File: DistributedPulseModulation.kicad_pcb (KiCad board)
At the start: 2 copper layers, 95.9 x 90.2 mm, 67 parts, among them J1 Conn_02x12_Odd_Even, J2 Conn_01x01, U1 74LS251, U10 4053, U11 4053, U12 4053, U2 74LVC2G74, U25 74LS85, U28 74LS85, U31 74LS85, U4 MCP23017_SP, U7 4053, U8 4040, U9 4040

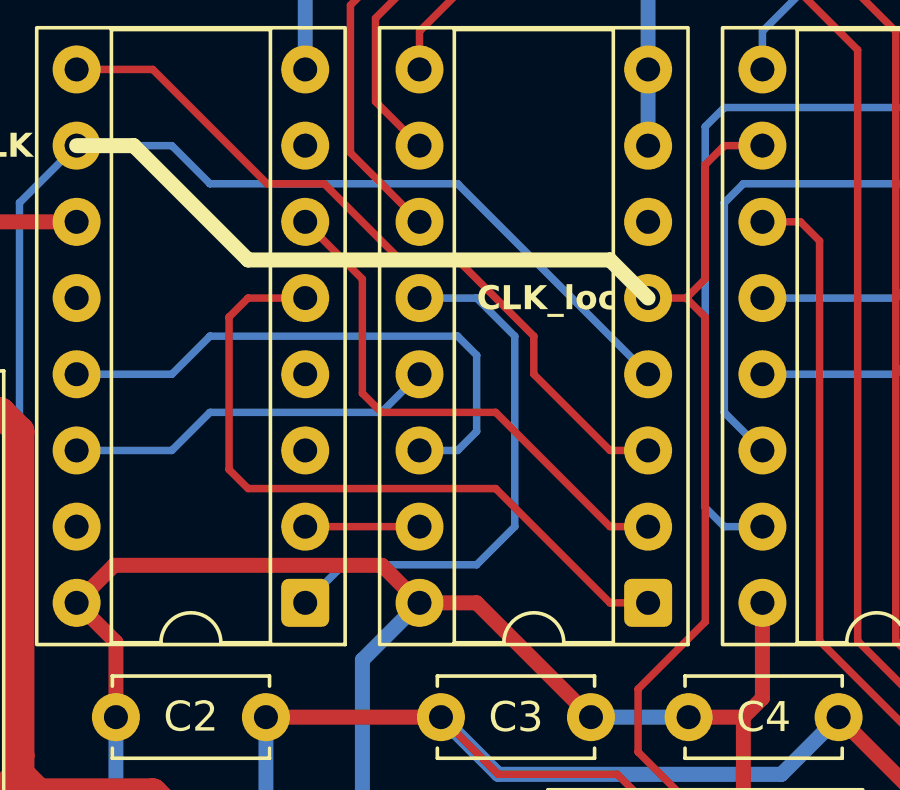
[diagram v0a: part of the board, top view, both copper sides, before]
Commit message: [UPGRADE] : ajout R6 pour pb tension entre TTL et CMOS - A jout de R6 (2.2K) en pull-uup sur la pin 5 du 74ls251 (TTL) en entrée du 74HCT4040 (CMOS)
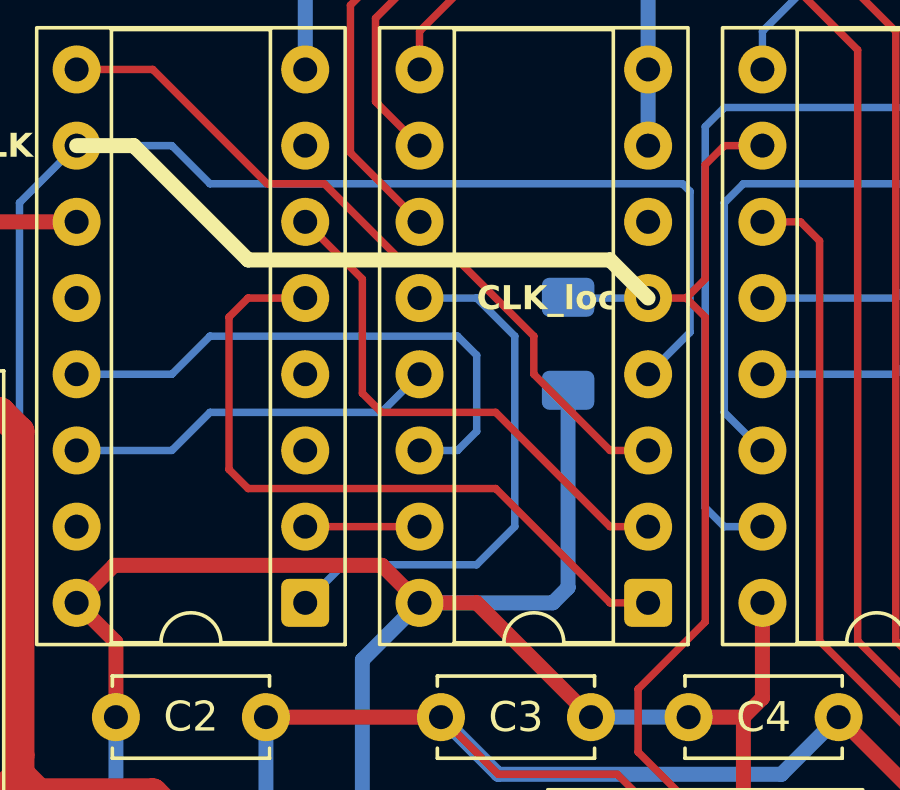
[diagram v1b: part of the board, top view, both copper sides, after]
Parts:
- added R6: 2.2K, Resistor_SMD:R_1206_3216Metric_Pad1.30x1.75mm_HandSolder, B.Cu at (69.1, 62.5)
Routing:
- net +5V: track 521.9 -> 533.6 mm
- net Clock: track 47.9 -> 53.5 mm
- net /Clock_loc: track 82.5 -> 85.2 mm

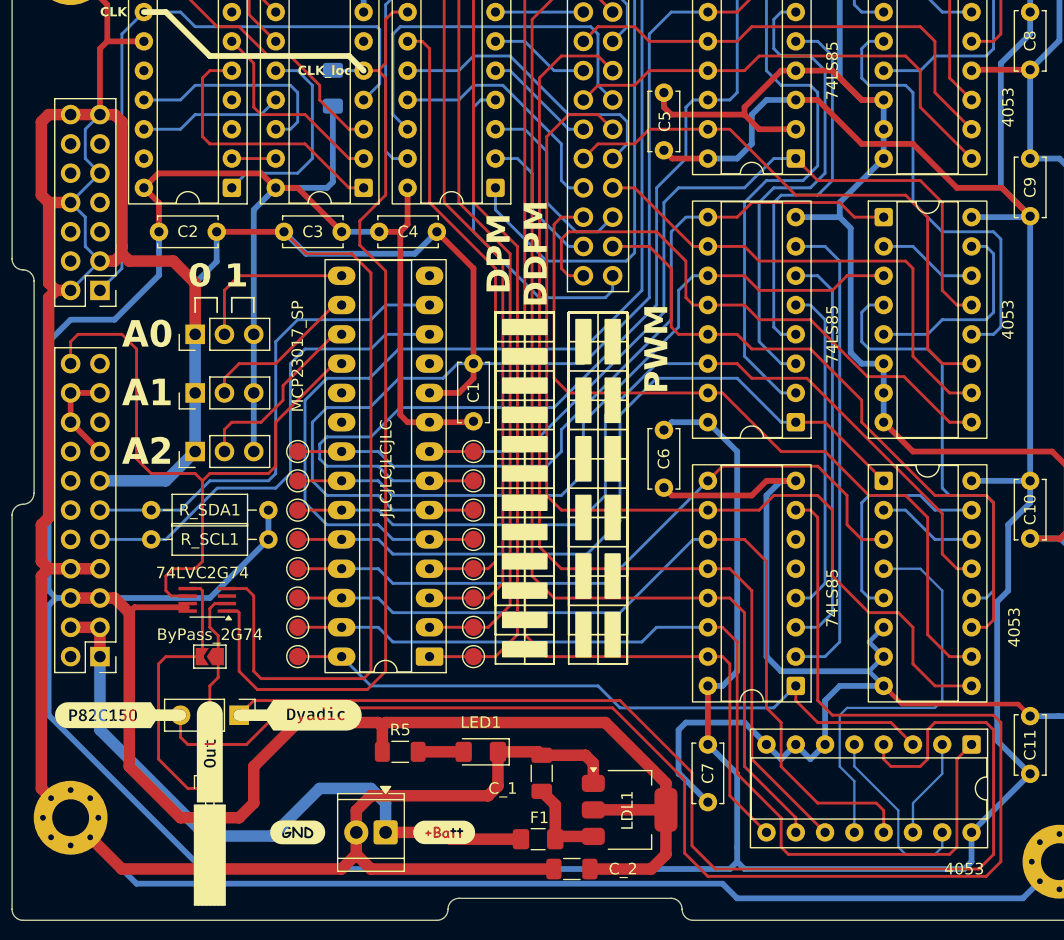
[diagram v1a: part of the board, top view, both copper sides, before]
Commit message: [UPGRADE] : ajout R7 pour pb tension entre TTL et CMOS - A jout de R7 (2.2K) en pull-up sur la sortie finale de la carte
[TODO]
-> adding replacement circuit for Dlatch chip
-> remove supply voltage regulator from PCB

[DONE]
-> correction voltage bugs
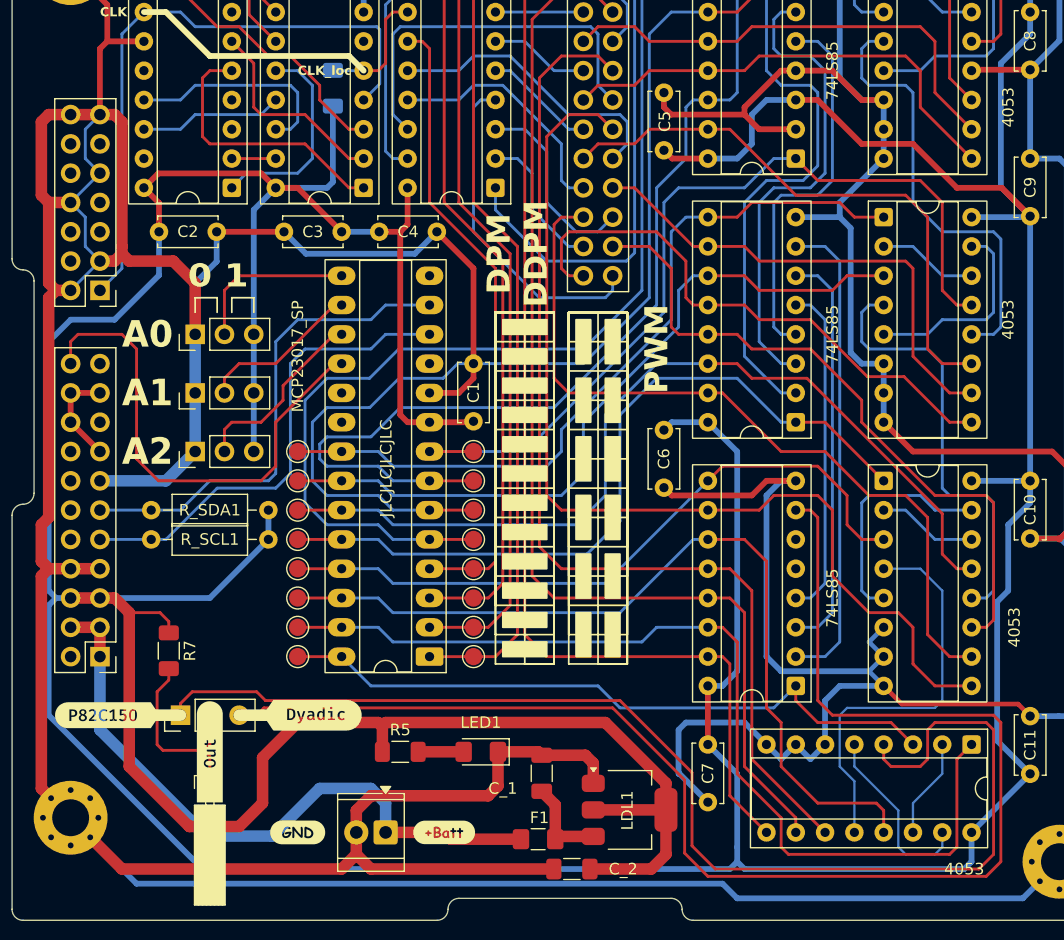
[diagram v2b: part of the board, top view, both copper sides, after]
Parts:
- removed ByPass_2G74: SolderJumper_2_Open, Jumper:SolderJumper-2_P1.3mm_Open_TrianglePad1.0x1.5mm
- removed U2: 74LVC2G74, Package_SO:SSOP-8_2.95x2.8mm_P0.65mm
- added R7: 2.2K, Resistor_SMD:R_1206_3216Metric_Pad1.30x1.75mm_HandSolder, F.Cu at (54.9, 111.3)
- moved JP5 5.08 mm to (55.9, 116.8), turned to 90 degrees
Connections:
- JP5 pad 2: Net-(ByPass_2G74-A) -> DPM
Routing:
- net /Clock_loc: track 85.2 -> 10.8 mm
- net Ground: track 881.5 -> 818.2 mm
- net ~{Reset}: track 57.0 -> 42.9 mm
- net Net-(ByPass_2G74-A): track 11.5 -> 0.00 mm
- net DPM_PWM: track 131.7 -> 123.4 mm
- net DPM: track 24.9 -> 18.0 mm
- net DDPM: track 101.4 -> 107.7 mm

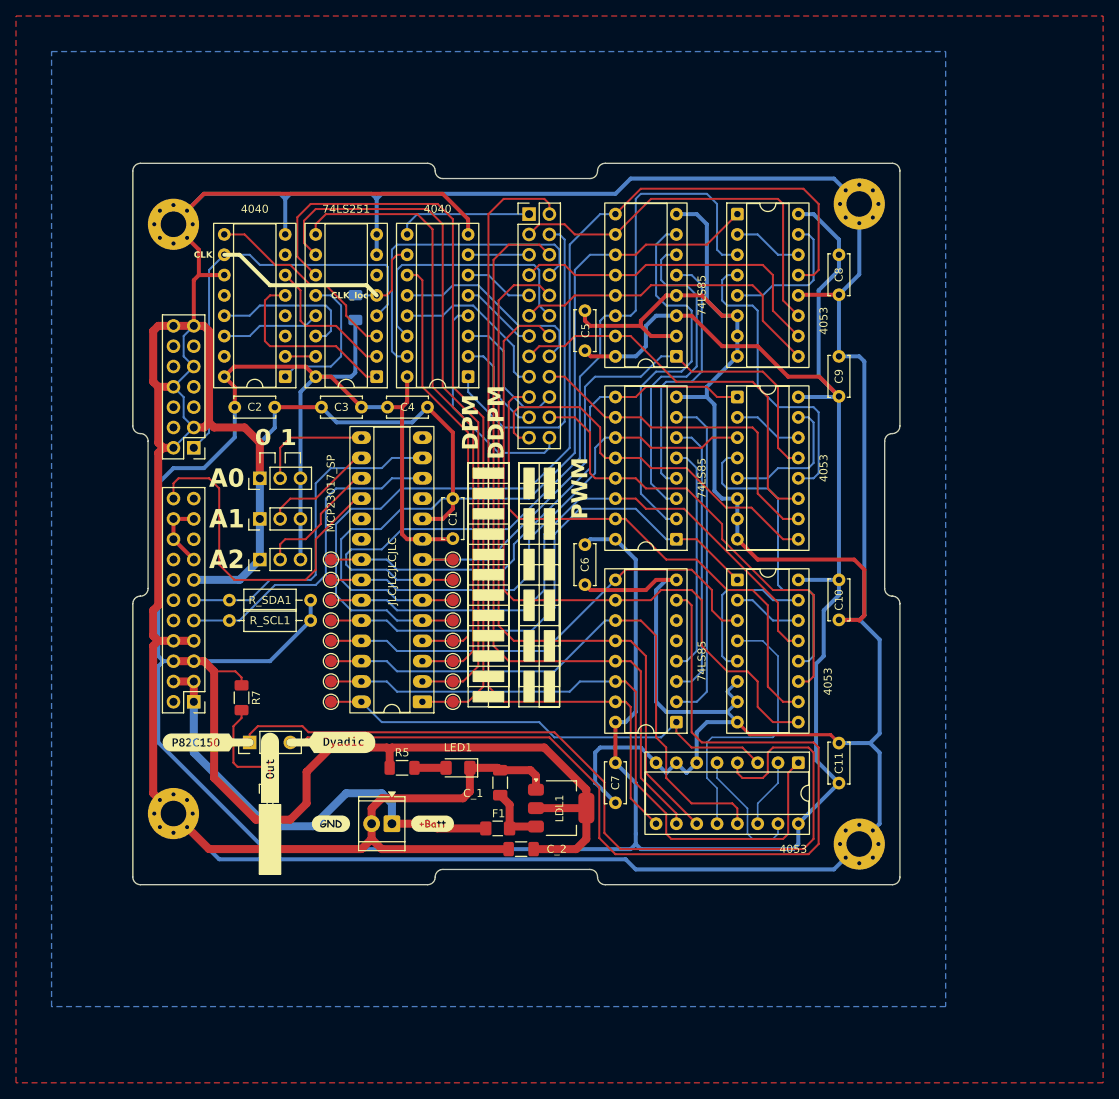
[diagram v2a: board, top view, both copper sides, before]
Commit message: [UPGRADE] : V2.1 in progress :-)
[DONE]
-> A jout de R7 (2.2K) en pull-up sur la sortie finale de la carte
-> A jout de R7 (2.2K) en pull-up sur la sortie clock locale
-> Bascule D sur sortie carte pour anti-rebond
-> retrait régulateur de tension
-> déplacement jumper d'adressage
-> ajout décodeur BCD vers 7 segment
-> ajout afficheur 7 segments sur l'addresse
-> détournement du "dot point" en tant que "power led"
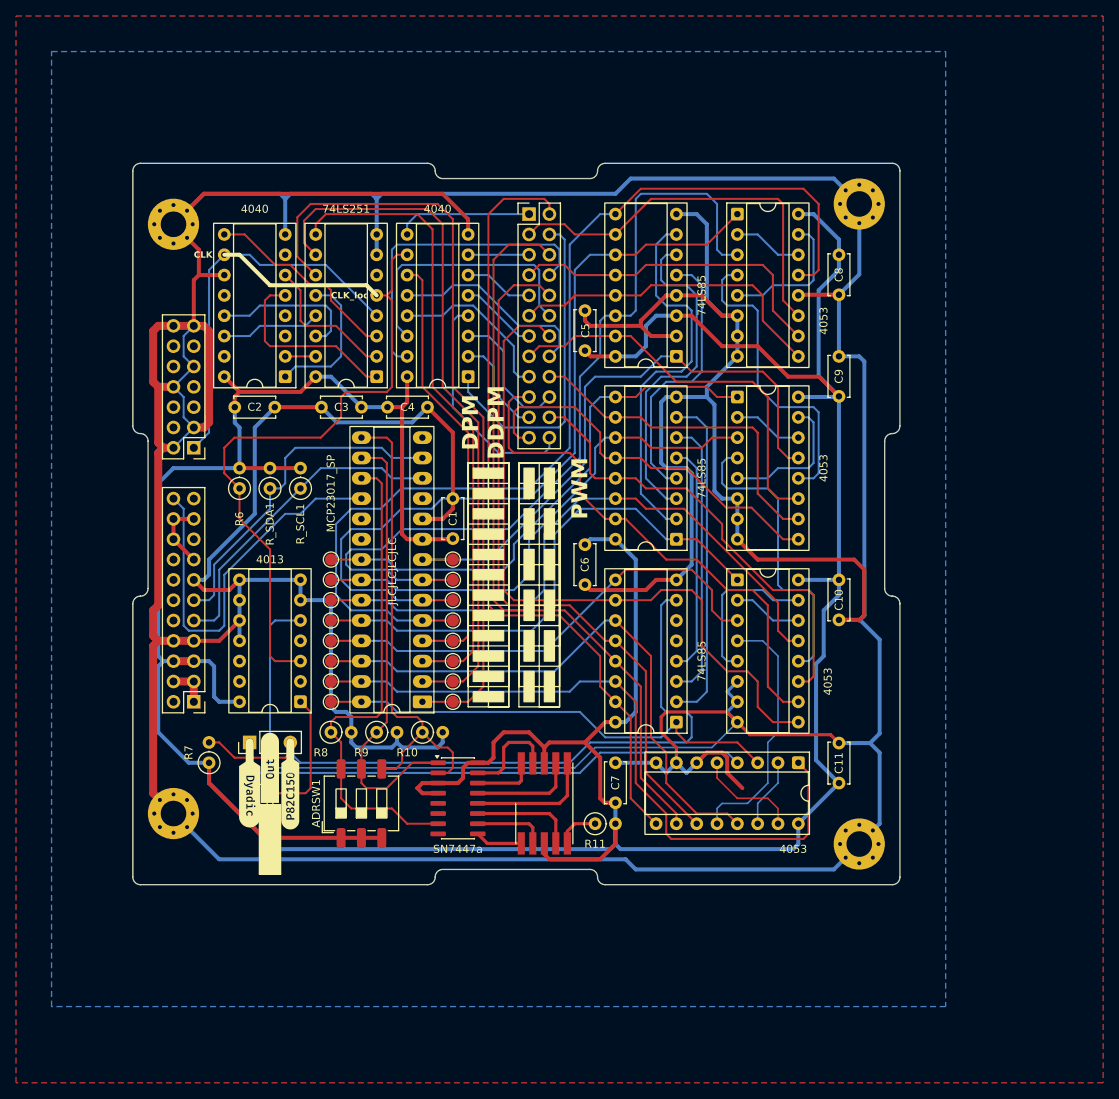
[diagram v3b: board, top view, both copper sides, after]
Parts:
- removed C_1, C_2: 4.7µF, Capacitor_SMD:C_1206_3216Metric_Pad1.33x1.80mm_HandSolder
- removed F1: .75A, Fuse:Fuse_1206_3216Metric_Pad1.42x1.75mm_HandSolder
- removed JP1, JP2, JP3: Jumper_3_Open, Connector_PinHeader_2.54mm:PinHeader_1x03_P2.54mm_Vertical
- removed J_VIN_0: Conn_01x02, TerminalBlock_TE-Connectivity:TerminalBlock_TE_282834-2_1x02_P2.54mm_Horizontal
- removed LDL1: LDL1117, Package_TO_SOT_SMD:SOT-223-3_TabPin2
- removed LED1: LED, LED_SMD:LED_1206_3216Metric_Pad1.42x1.75mm_HandSolder
- removed R5: 1K, Resistor_SMD:R_1206_3216Metric_Pad1.30x1.75mm_HandSolder
- removed kibuzzard-680E1E0B: G***, kibuzzard-680E1E0B
- removed kibuzzard-680E1E1F: G***, kibuzzard-680E1E1F
- removed kibuzzard-680E6C5F: G***, kibuzzard-680E6C5F
- added ADRSW1: SW_DIP_x03, Button_Switch_SMD:SW_DIP_SPSTx03_Slide_6.7x9.18mm_W8.61mm_P2.54mm_LowProfile, F.Cu at (69.8, 124.5)
- added DS1: GS2011CR-G, Display_7Segment:KCSC02-105, F.Cu at (92.7, 124.5)
- added IC1: SN7447a, Package_SO:SOIC-16_3.9x9.9mm_P1.27mm, F.Cu at (81.9, 123.8)
- added R10: 2.2K, Resistor_THT:R_Axial_DIN0207_L6.3mm_D2.5mm_P2.54mm_Vertical, F.Cu at (77.5, 115.6)
- added R11: 2.2K, Resistor_THT:R_Axial_DIN0207_L6.3mm_D2.5mm_P2.54mm_Vertical, F.Cu at (99.1, 127.0)
- added R8: 2.2K, Resistor_THT:R_Axial_DIN0207_L6.3mm_D2.5mm_P2.54mm_Vertical, F.Cu at (66.0, 115.6)
- added R9: 2.2K, Resistor_THT:R_Axial_DIN0207_L6.3mm_D2.5mm_P2.54mm_Vertical, F.Cu at (71.8, 115.6)
- added U2: 4013, Package_DIP:DIP-14_W7.62mm_Socket, F.Cu at (62.2, 111.8)
- added kibuzzard-6A7A12BF: G***, kibuzzard-6A7A12BF, B.Cu at (89.5, 99.7)
- R6: footprint Resistor_SMD:R_1206_3216Metric_Pad1.30x1.75mm_HandSolder -> Resistor_THT:R_Axial_DIN0207_L6.3mm_D2.5mm_P2.54mm_Vertical; moved to F.Cu
- R7: footprint Resistor_SMD:R_1206_3216Metric_Pad1.30x1.75mm_HandSolder -> Resistor_THT:R_Axial_DIN0207_L6.3mm_D2.5mm_P2.54mm_Vertical
- R_SCL1, R_SDA1: footprint Resistor_THT:R_Axial_DIN0207_L6.3mm_D2.5mm_P10.16mm_Horizontal -> Resistor_THT:R_Axial_DIN0207_L6.3mm_D2.5mm_P2.54mm_Vertical
- moved R6 26.8 mm to (54.6, 85.1)
- moved R_SCL1 18.8 mm to (62.2, 85.1), turned to 90 degrees
- moved R_SDA1 14.9 mm to (58.4, 85.1), turned to 90 degrees
- moved kibuzzard-68110930 13.1 mm to (61.0, 123.2), turned to 90 degrees
- moved kibuzzard-6811091F 13.1 mm to (55.9, 123.2), turned to -90 degrees
- moved R7 9.09 mm to (50.8, 119.4), turned to 90 degrees
- moved C7 5.00 mm to (101.6, 119.4), turned to -90 degrees
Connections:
- net VBatt renamed /Bus de fond panier/+Batt
- JP5 pad 2: DPM -> Net-(JP5-C)
- R6 pad 1: +5V -> /Clock_loc
- R6 pad 2: /Clock_loc -> +5V
- R7 pad 2: DPM -> DPM_PWM
- U4 pad 15: Net-(JP3-C) -> /ADR2
- U4 pad 16: Net-(JP2-C) -> /ADR1
- U4 pad 17: Net-(JP1-C) -> /ADR0
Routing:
- net /Clock_loc: track 10.8 -> 77.9 mm
- net /ADR0: track 0.00 -> 61.1 mm
- net /ADR2: track 0.00 -> 59.9 mm
- net +5V: track 534.1 -> 475.3 mm
- net /ADR1: track 0.00 -> 55.9 mm
- net /Bus de fond panier/+Batt: track 56.8 -> 5.08 mm
- net Ground: track 818.2 -> 866.4 mm
- net DDPM: track 107.7 -> 66.0 mm
- net DPM_PWM: track 123.4 -> 87.5 mm
- net Net-(JP5-C): track 0.00 -> 18.7 mm
- net Net-(JP1-C): track 16.2 -> 0.00 mm
- net Net-(DS1-b): track 0.00 -> 15.6 mm
- net Net-(JP3-C): track 14.5 -> 0.00 mm
- net Net-(JP2-C): track 14.1 -> 0.00 mm
- net Net-(DS1-c): track 0.00 -> 13.0 mm
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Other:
- board text added: "Used only for the clock signal"
- board text removed: "0 1"
- board text removed: "A0"
- board text removed: "A1"
- board text removed: "A2"
- board text removed: "Optionnal bus for CanDuino128"
